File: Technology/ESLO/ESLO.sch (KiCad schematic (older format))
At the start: 47 parts, among them J1 USB_B_Micro, J2 nRF24L01+, J3 Ibatt, J4 Board to Board, J5 Conn_01x10_Female, J6 Board to Board, SW1 RESET, U1 MAX1720, U10 ADS1294, U11 ATSAMD21G18A-AUT, U2 LP5907MFX-1.8, U3 LP5907MFX-3.0, U4 LP5907MFX-1.5, U5 TPS72301DDCT, U6 SN74AUP1G98, U7 MB85RS2MT, U8 MT29F2G01ABBGDWB-IT:G TR, U9 LSM303AGR, Y1 Crystal

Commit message: ESLO changelog
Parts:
- removed BT1: Coin Cell, Battery:BatteryHolder_Keystone_1058_1x2032, symbol Device:Battery_Cell
- removed C14: 100nF, Capacitor_SMD:C_0402_1005Metric, symbol Device:C
- removed C2, C5: 1uF, Capacitor_SMD:C_0402_1005Metric, symbol Device:C
- removed D1: LED, LED_SMD:LED_0603_1608Metric, symbol Device:LED
- removed J1: USB_B_Micro, Connector_USB:USB_Micro-B_Molex-105017-0001, symbol Connector:USB_B_Micro
- removed J2: nRF24L01+, Connector_PinHeader_2.54mm:PinHeader_2x04_P2.54mm_Vertical, symbol Connector_Generic:Conn_02x04_Odd_Even
- removed J3: Ibatt, TerminalBlock_4Ucon:TerminalBlock_4Ucon_1x02_P3.50mm_Horizontal, symbol Connector:Screw_Terminal_01x02
- removed J4: Board to Board, Connector_Hirose:Hirose_DF52-6S-0.8H_1x06-1MP_P0.80mm_Horizontal, symbol Connector:Conn_01x06_Female
- removed JP1: Jumper, Connector_PinHeader_2.54mm:PinHeader_1x02_P2.54mm_Vertical, symbol Device:Jumper
- removed R1, R2: 4.7k, Resistor_SMD:R_0402_1005Metric, symbol Device:R
- removed SW1: RESET, Button_Switch_SMD:SW_SPST_B3S-1000, symbol Switch:SW_Push
- removed U3: LP5907MFX-3.0, Package_TO_SOT_SMD:SOT-23-5, symbol Regulator_Linear:LP5907MFX-3.0
- added C16, C18, C20, C27, C32, C34, C35: 1uF, Capacitor_SMD:C_0402_1005Metric, symbol Device:C
- added C17, C19, C21, C28, C33: 0.1uF, Capacitor_SMD:C_0402_1005Metric, symbol Device:C
- added C22, C23, C25, C26: 4.7nF, Capacitor_SMD:C_0402_1005Metric, symbol Device:C
- added C24: 1000pF, Capacitor_SMD:C_0402_1005Metric, symbol Device:C
- added C29: 10nF, Capacitor_SMD:C_0402_1005Metric, symbol Device:C
- added C30, C36: 1nF, Capacitor_SMD:C_0402_1005Metric, symbol Device:C
- added C31: 22uF, Capacitor_SMD:C_0603_1608Metric, symbol Device:C
- added C37: 4.7pF, Capacitor_SMD:C_0402_1005Metric, symbol Device:C
- added C38: 2.2nF, Capacitor_SMD:C_0402_1005Metric, symbol Device:C
- added C39: 1.5pF, Capacitor_SMD:C_0402_1005Metric, symbol Device:C
- added C40: 1pF, Capacitor_SMD:C_0402_1005Metric, symbol Device:C
- added C41: 33nF, Capacitor_SMD:C_0402_1005Metric, symbol Device:C
- added C42, C43: 22pF, Capacitor_SMD:C_0402_1005Metric, symbol Device:C
- added L1: 2.7nH, Inductor_SMD:L_0402_1005Metric, symbol Device:L
- added L2: 8.2nH, Inductor_SMD:L_0402_1005Metric, symbol Device:L
- added L3: 3.9nH, Inductor_SMD:L_0402_1005Metric, symbol Device:L
- added NT1: Net-Tie_2, NetTie:NetTie-2_SMD_Pad0.5mm, symbol Device:Net-Tie_2
- added R10, R11, R12, R14, R15: 4.7k, LED_SMD:LED_0402_1005Metric, symbol Device:R
- added R13: 1M, LED_SMD:LED_0402_1005Metric, symbol Device:R
- added R16, R17, R18, R7: 4.7k, Resistor_SMD:R_0402_1005Metric, symbol Device:R
- added R19: 22k, LED_SMD:LED_0402_1005Metric, symbol Device:R
- added R4, R5, R9: 100k, LED_SMD:LED_0402_1005Metric, symbol Device:R
- added U11: nRF24L01P, Package_DFN_QFN:QFN-20-1EP_4x4mm_P0.5mm_EP2.5x2.5mm, symbol RF:nRF24L01P
- added U12: AN91445, ARBO Parts:AN91445_MG, symbol ARBO_library:AN91445_MG
- added Y2: SXT21412AA16, MyAntennas:SXT214, symbol Device:Crystal_GND24_Small
- U8: renamed from U7; value MB85RS2MT -> CY15V104QI-20LPXC
- renumbered C3 to C1, C9 to C11, C11 to C13, C12 to C14, C13 to C15, C6 to C2, C8 to C3, C15 to C4, C16 to C5, C17 to C6, C1 to C7, C4 to C8, C7 to C9, D2 to D1, J6 to J1, J5 to J2, R5 to R1, R6 to R2, R7 to R3, R3 to R6, R4 to R8, U2 to U1, U6 to U10, U4 to U2, U8 to U3, U1 to U4, U11 to U6, U9 to U7, U10 to U9
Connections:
- net +1V8: now also U9.8B (CLKSEL), U9.8C (DVDD), U9.8D (DVDD), C18.2, C19.2, R9.1
- net +BATT: now also R4.1
- net EEG_CS: now also U9.7F (~CS)
- net GNDA: now also C16.2, C17.2, C18.1, C19.1, C27.2, C28.2, NT1.2; no longer C1.2, C13.2, C14.2, C15.1, C4.2, C5.1, C6.1, J1.6 (Pin_6), R1.2, U1.2 (GND), U10.2 (GND), U3.4 (Vss), U6.18 (GND), U6.35 (GND), U6.42 (GND), U6.5 (GNDANA), U7.6 (GND), U7.8 (GND), U8.4 (GND)
- net MISO: now also U6.21 (PA12/MISO), U9.8E (DOUT), U11.5 (MISO)
- net MOSI: now also U9.8H (DIN), U11.4 (MOSI)
- net RF_CE: now also U11.1 (CE)
- net RF_IRQ: now also U11.6 (IRQ)
- net R_VBATT: now also R4.2, R5.1
- net SCK: now also U11.3 (SCK)
- net VDDA: now also U9.4A (AVDD), U9.4B (AVDD), U9.6A (AVDD), U9.6B (AVDD), U9.6C (AVDD), U9.7A (AVDD1), C16.1, C17.1
- net VSSA: now also U9.4D (AVSS), U9.4H (VREFN), U9.5A (AVSS), U9.5B (AVSS), U9.5C (AVSS), U9.5D (AVSS), U9.8A (AVSS1), C20.1, C21.1, C27.1, C28.1, C31.2, C32.2, C33.2, C34.2, C35.2, C36.2
- net ~SHDN: now also U9.5G (~PWDN), U9.6G (~RESET), R7.1
- net TEMP: now reaches U6.3 (PA02/A0)
- net TEMP: now also J1.4 (Pin_4), R9.2
- net at U9.1E (IN4P): now also C22.1, R10.1
- net at U9.1F (IN3P): now also C23.1, R12.1
- net at U9.1G (IN2P): now also C25.1, R15.1
- net at U9.1H (IN1P): now also C26.1, R17.1
- net at U9.2E (IN4N): now also C22.2, R11.1
- net at U9.2F (IN3N): now also C23.2, R14.1
- net at U9.2G (IN2N): now also C25.2, R16.1
- net at U9.2H (IN1N): now also C26.2, R18.1
- net at U9.3A (RLDIN): now also J2.10 (Pin_10), U9.3B (RLDOUT), C24.1, R13.1
- net at U9.3C (RLDINV): now also C24.2, R13.2
- net at U9.3D (WCT): now also C36.1
- net at U9.3G (VCAP4): now also C35.1
- net at U9.3H (VREFP): now also C20.2, C21.2
- net GNDD: now reaches U9.4E (RESV1)
- net GNDD: now also C1.2, C13.2, C14.2, C15.1, C4.2, C5.1, C6.1, J1.6 (Pin_6), R1.2, U1.2 (GND), U10.2 (GND), U3.4 (Vss), U6.18 (GND), U6.35 (GND), U6.42 (GND), U6.5 (GNDANA), U7.6 (GND), U7.8 (GND), U8.4 (GND), U9.6F (DAISY_IN), U9.7C (DGND), U9.7D (DGND), U9.7H (DGND), C29.2, C30.2, C37.2, C38.2, C40.1, C41.1, C42.2, C43.2, NT1.1, R19.2, R5.2, R7.2, U11.14 (VSS), U11.17 (VSS), U11.20 (VSS), U11.8 (VSS), Y2.2, Y2.4
- net at U9.5H (VCAP1): now also C31.1
- net EEG_DRDY: now reaches U9.6D (~DRDY)
- net at U9.6H (VCAP2): now also C32.1
- net at U9.7B (VCAP3): now also C33.1, C34.1
- net EEG_START: now reaches U9.7G (START)
- net at U9.8F (SCLK): now also U10.4 (Y)
- net at J2.1 (Pin_1): now also R17.2
- net at J2.2 (Pin_2): now also R18.2
- net at J2.3 (Pin_3): now also R15.2
- net at J2.4 (Pin_4): now also R16.2
- net at J2.5 (Pin_5): now also R12.2
- net at J2.6 (Pin_6): now also R14.2
- net at J2.7 (Pin_7): now also R10.2
- net at J2.8 (Pin_8): now also R11.2
- new net: C39.2, C40.2, U12.1 (SIG)
- new net: C43.1, U11.10 (XC1), Y2.3
- new net: C37.1, C38.1, L1.2, U11.11 (VDD_PA)
- new net: L1.1, L2.1, U11.12 (ANT1)
- new net: L2.2, L3.1, U11.13 (ANT2)
- new net: C29.1, C30.1, U11.15 (VDD), U11.18 (VDD), U11.7 (VDD)
- new net: R19.1, U11.16 (IREF)
- new net: C41.2, U11.19 (DVDD)
- new net: C42.1, U11.9 (XC2), Y2.1
- new net: C39.1, L3.2
- new net RF_CSN: U11.2 (CSN)
- no-connect marks 5 -> 6
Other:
- note added: "Debug line"
- note added: "START req?"
- note removed: "5 = debug"
- note removed: "Debug"
- note removed: "Vbatt"
- moved on the sheet: J2, U10, U9

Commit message: Added ESLO debugger and PSP
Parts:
- added TP1, TP2: TestPoint, TestPoint:TestPoint_Pad_D1.0mm, symbol Connector:TestPoint
- C1, C16, C18, C2, C20, C27, C3, C32, C34, C35, C6, C7, C8: Digikey (none) -> 399-4873-1-ND
- C10, C9: Digikey (none) -> 490-10451-1-ND
- C11, C29: Digikey (none) -> 490-6326-2-ND
- C13: value 100nF -> 0.1uF; Digikey (none) -> 490-6328-1-ND
- C15: Digikey (none) -> 490-14372-1-ND
- C17, C19, C21, C28, C33: Digikey (none) -> 490-6328-1-ND
- C22, C23, C25, C26, C37: Digikey (none) -> 490-5874-2-ND
- C24, C30, C36: Digikey (none) -> 490-6350-2-ND
- C38: Digikey (none) -> 311-1037-1-ND
- C39: Digikey (none) -> 490-6212-2-ND
- C4, C42, C43, C5: Digikey (none) -> 311-1652-1-ND
- C40: Digikey (none) -> 490-6206-2-ND
- C41: Digikey (none) -> 490-11984-2-ND
- D1: Digikey (none) -> 732-4971-1-ND
- J1: Digikey (none) -> H125100CT-ND
- J2: Digikey (none) -> H125102CT-ND
- L1: Digikey (none) -> 2035-0402HP-2N7EJTSCT-ND
- L2: Digikey (none) -> 2035-1500-1-ND
- L3: Digikey (none) -> 2035-0402HS-3N9EGTSCT-ND
- R1, R16, R17, R18, R2, R3, R7: Digikey (none) -> 311-4.7KJRCT-ND
- R10, R11, R12, R14, R15: footprint LED_SMD:LED_0402_1005Metric -> Resistor_SMD:R_0402_1005Metric; Digikey (none) -> 311-4.7KJRCT-ND
- R13: footprint LED_SMD:LED_0402_1005Metric -> Resistor_SMD:R_0402_1005Metric; Digikey (none) -> 311-1.00MLRCT-ND
- R19: footprint LED_SMD:LED_0402_1005Metric -> Resistor_SMD:R_0402_1005Metric; Digikey (none) -> 311-22.0KLRCT-ND
- R4, R5, R9: Digikey (none) -> 311-100KLRCT-ND
- U1: Digikey (none) -> 296-42463-1-ND
- U11: Digikey (none) -> 1490-1033-1-ND
- U4: Digikey (none) -> MAX1720EUTGOSCT-ND
- U8: footprint Package_DFN_QFN:DFN-8-1EP_3x3mm_P0.65mm_EP1.7x2.05mm -> ARBO Parts:8-GQFN_FRAM_3.28mm-3.23mm; Digikey (none) -> 428-4724-ND
- Y2: Digikey (none) -> 2388-SXT21412AA16-16.000M-ND
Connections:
- net +BATT: now also C29.1, C30.1, U11.15 (VDD), U11.18 (VDD), U11.7 (VDD)
- net EEG_CS: now also U6.15 (PA10/D1)
- net EEG_DRDY: now also U6.16 (PA11/D0)
- net EEG_START: now also U6.22 (PA13/D38)
- net FRAM_CS: now also U6.13 (PA08/D4)
- net GNDD: now also U12.2 (GND)
- net INT1_XL: now also U6.30 (PA21/D7)
- net INT2_XL: now also U6.29 (PA20/~D6)
- net MAG_INT: now also U6.28 (PA19/~D12)
- net NAND_CS: now also U6.14 (PA09/D3)
- net RF_CE: now also U6.24 (PA15/~D5)
- net RF_CSN: now also U6.23 (PA14/D2/XIN)
- net RF_IRQ: now also U6.25 (PA16/~D11)
- net SWCLK: now also TP1.1
- net SWDIO: now also TP2.1
- net TEMP: now also U6.10 (PA05/A4); no longer U6.3 (PA02/A0)
- net ~SHDN: now also U6.11 (PA06/D8/A6)
- net DEBUG: now reaches U6.27 (PA18/~D10)
- net DEBUG: now also J1.5 (Pin_5)
- net D-: now reaches J1.2 (Pin_2), U6.33 (PA24/D-)
- net D+: now reaches J1.3 (Pin_3), U6.34 (PA25/D+)
- no-connect marks 6 -> 18
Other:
- note removed: "10uF–rec. aluminum"
- moved on the sheet: J1, R7, R9

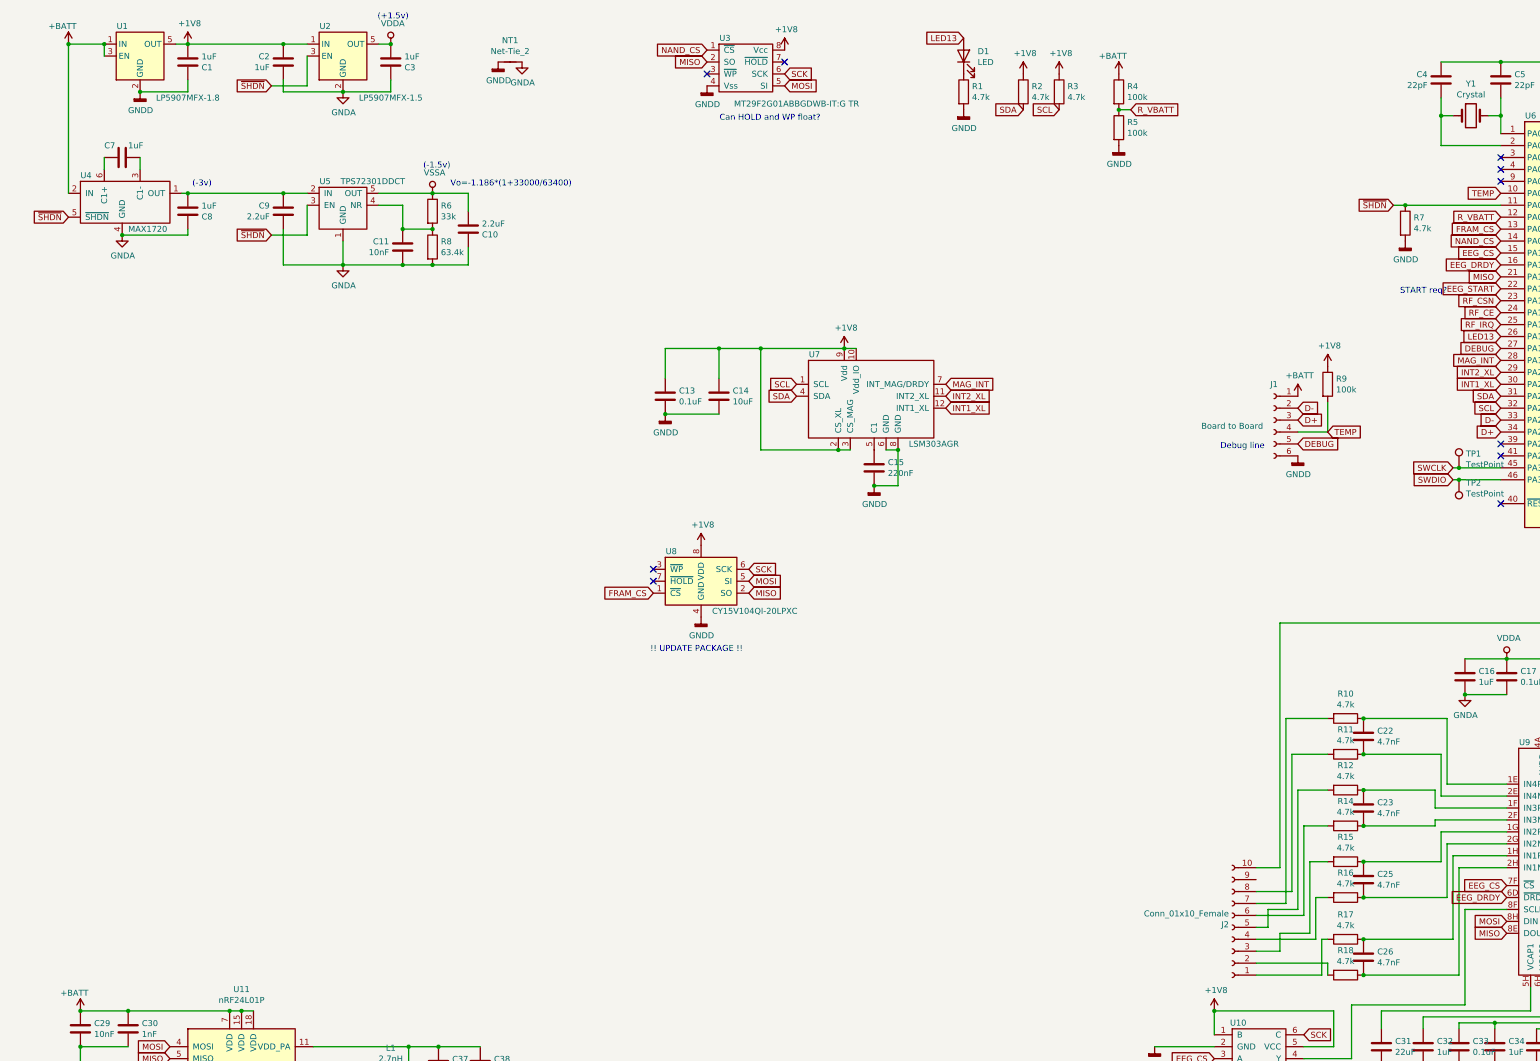
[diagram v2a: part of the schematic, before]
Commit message: Reconsidering ESLO architecture (-> CC2640R2)
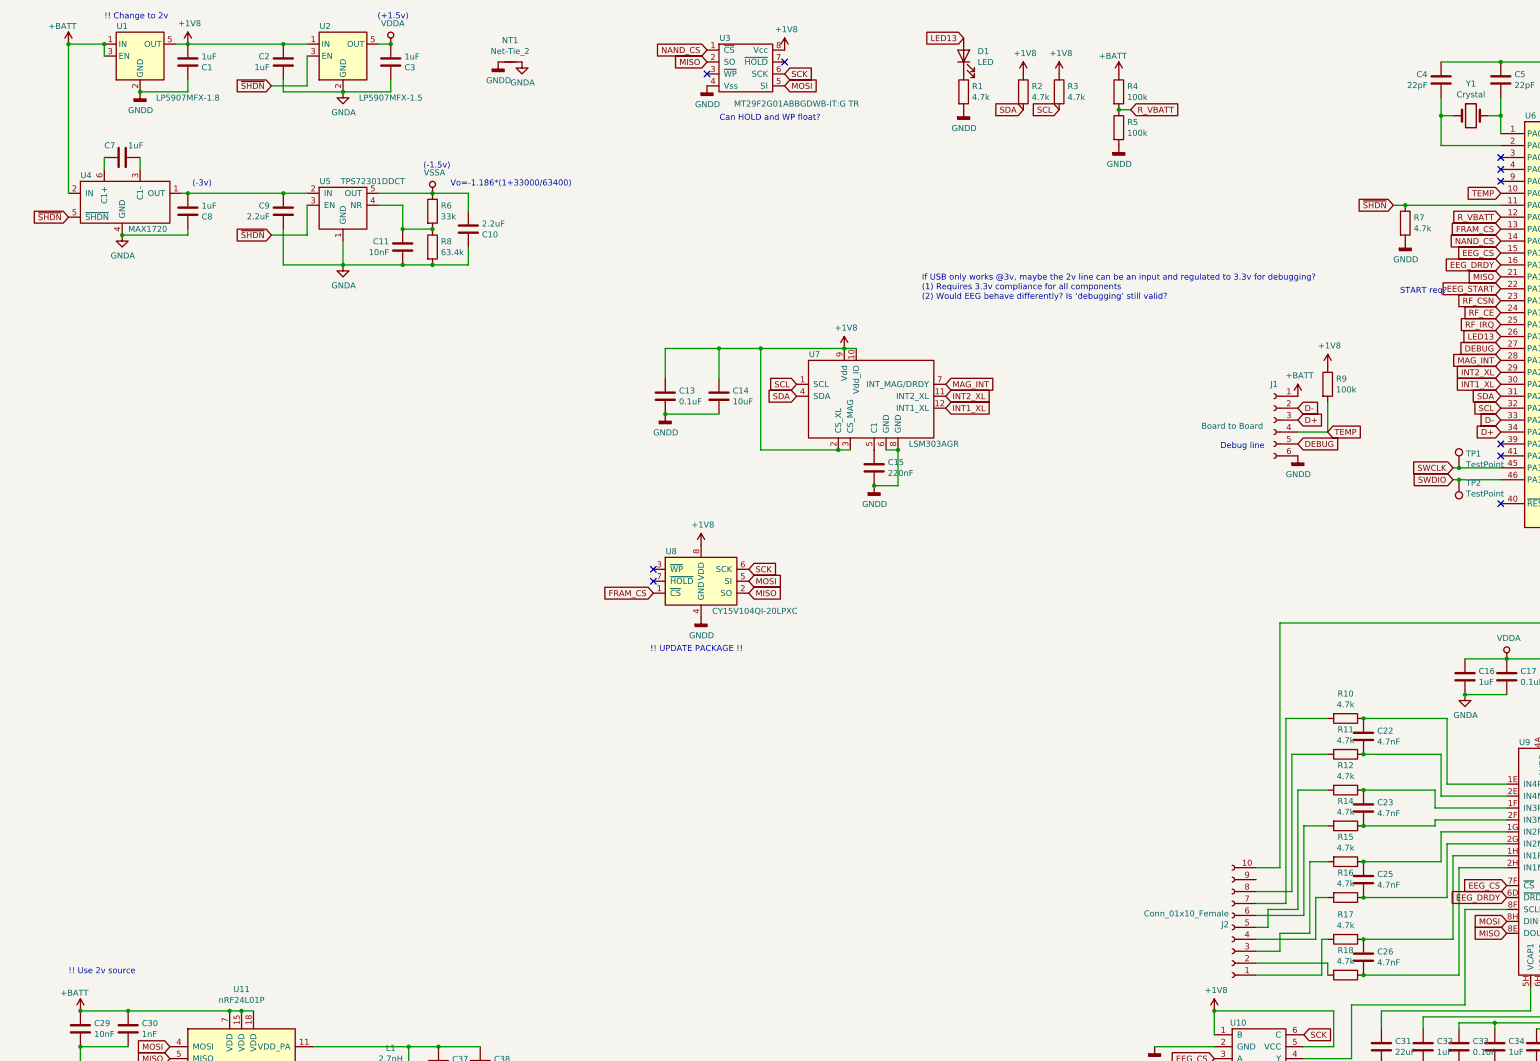
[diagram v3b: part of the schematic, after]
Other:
- note added: "!! Change to 2v"
- note added: "!! Use 2v source"
- note added: "If USB only works @3v, maybe the 2v line can be an input and regulated to 3.3v for debugging? \n(1) Requires 3.3v compliance for all components\n(2) Would EEG behave differently? Is ‘debugging’ still valid?"
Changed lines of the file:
@@
 Wire Wire Line
 	12600 4550 12950 4550
+Text Notes 950  8700 0    50   ~ 0
+!! Use 2v source
+Text Notes 1250 700  0    50   ~ 0
+!! Change to 2v
+Text Notes 8100 3050 0    50   ~ 0
+If USB only works @3v, maybe the 2v line can be an input and regulated to 3.3v for debugging? \n(1) Requires 3.3v compliance for all components\n(2) Would EEG behave differently? Is ‘debugging’ still valid?
 $EndSCHEMATC
